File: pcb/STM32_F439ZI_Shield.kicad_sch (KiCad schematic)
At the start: 27 parts, among them J3 Relais_Conn, J4 Conn_01x02_Pin, J5 Conn_01x02_Pin, K1 G6S-2, K2 G6S-2, U1 LM2904, U12 FL25L16B, U13 R-78E-5.0-1.0, U2 MAX3485

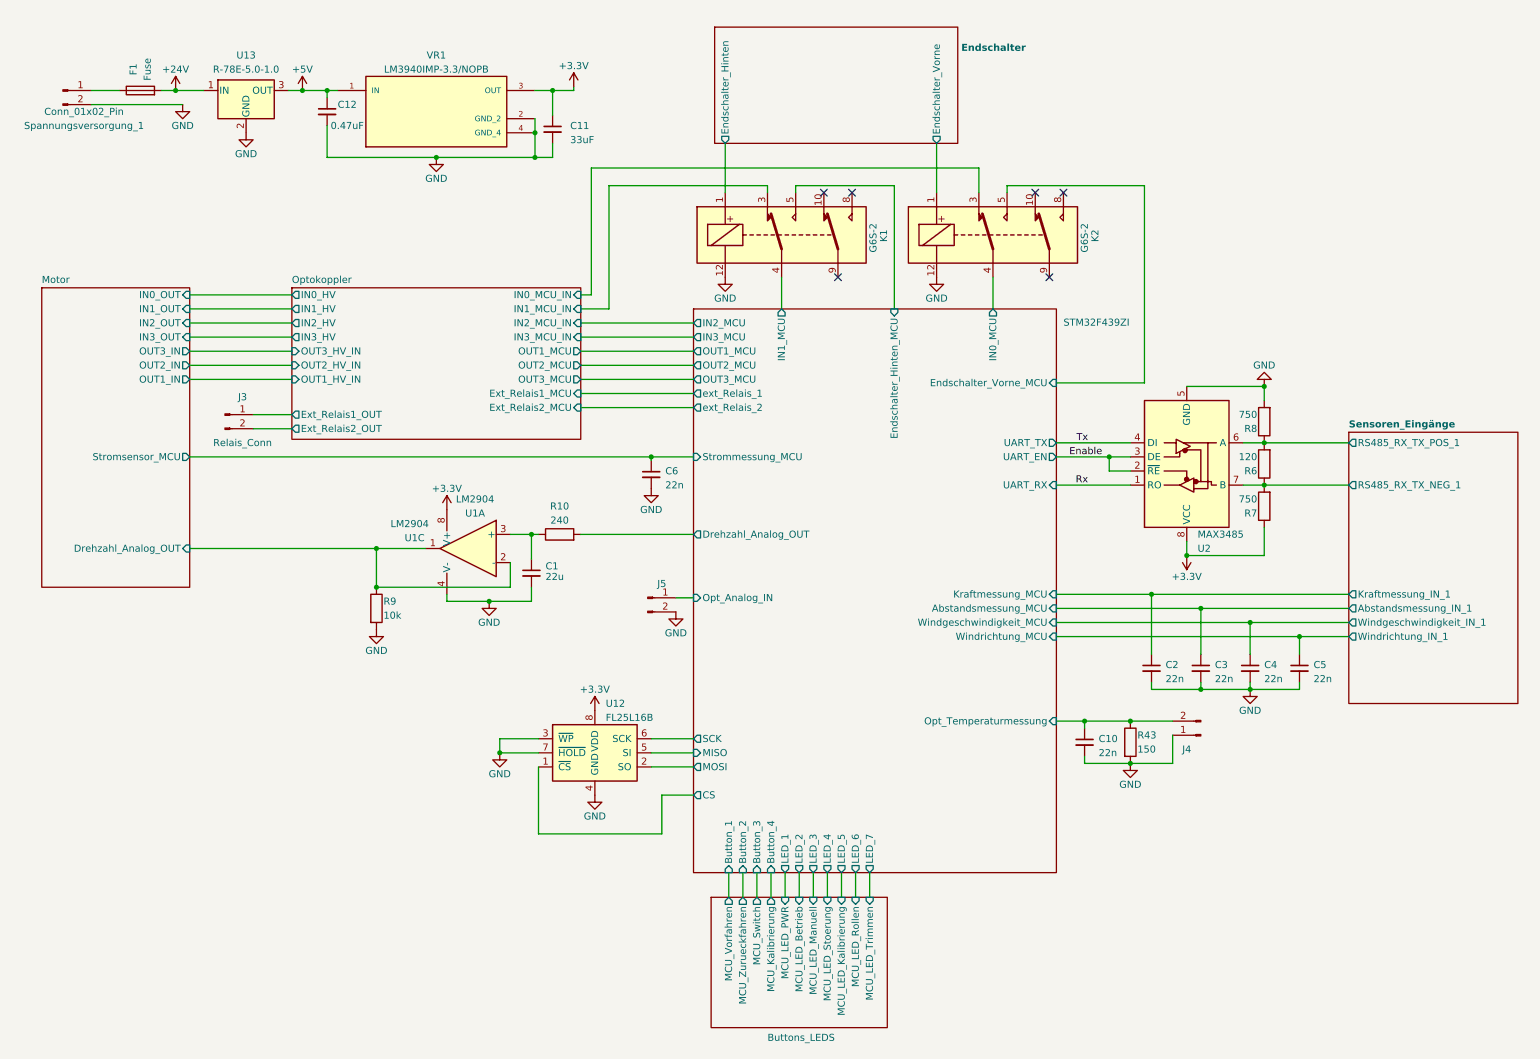
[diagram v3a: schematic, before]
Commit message: finished assigning pins and creating pcb
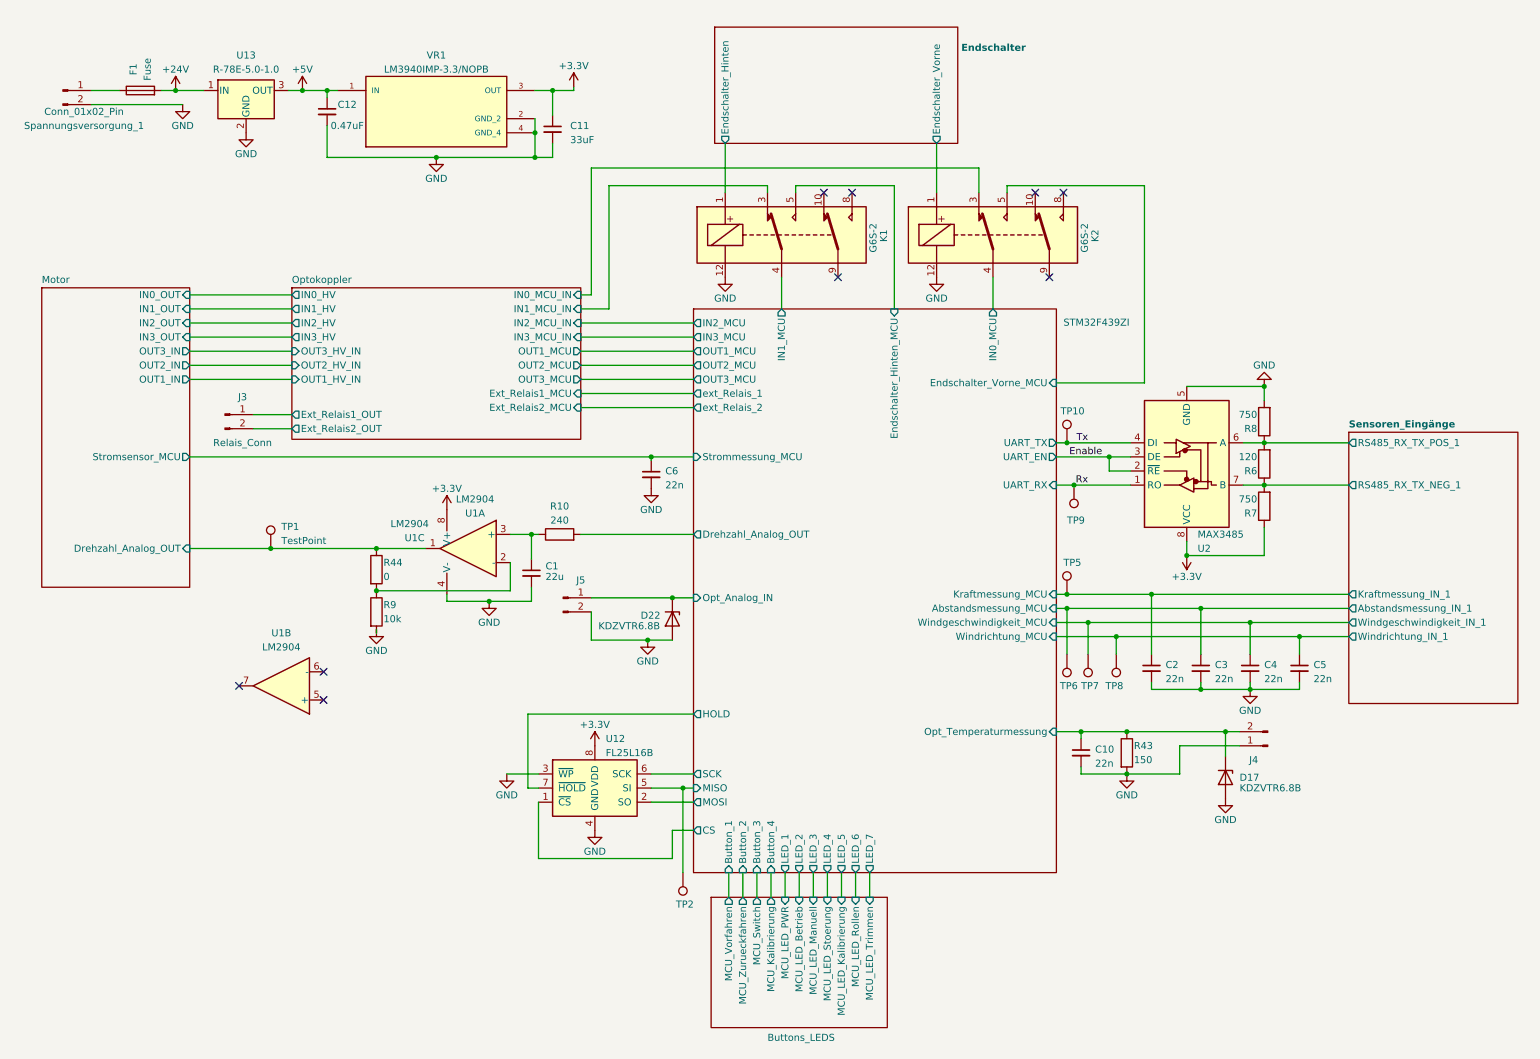
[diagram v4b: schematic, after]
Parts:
- added D17, D22: KDZVTR6.8B, Diode_SMD:D_SOD-123, symbol Diode:Z2SMBxxx
- added R44: 0, Resistor_SMD:R_1206_3216Metric, symbol Device:R
- added TP1, TP10, TP2, TP5, TP6, TP7, TP8, TP9: TestPoint, TestPoint:TestPoint_THTPad_2.0x2.0mm_Drill1.0mm, symbol Connector:TestPoint
- added unit 2 of U1
- Spannungsversorgung_1: footprint TerminalBlock_TE-Connectivity:TerminalBlock_TE_282834-2_1x02_P2.54mm_Horizontal -> TerminalBlock_Phoenix:TerminalBlock_Phoenix_PT-1,5-2-3.5-H_1x02_P3.50mm_Horizontal
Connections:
- net GND: now also D17.2 (A), D22.2 (A); no longer U12.7 (~{HOLD})
- net Motor/Drehzahl_Analog_OUT: now also R44.1, TP1.1; no longer R9.1, U1.2 (-)
- net Rx: now also TP9.1
- net STM32F439ZI/Abstandsmessung_MCU: now also TP6.1
- net STM32F439ZI/Kraftmessung_MCU: now also TP5.1
- net STM32F439ZI/MISO: now also TP2.1
- net STM32F439ZI/Opt_Analog_IN: now also D22.1 (K)
- net STM32F439ZI/Opt_Temperaturmessung: now also D17.1 (K)
- net STM32F439ZI/Windgeschwindigkeit_MCU: now also TP7.1
- net STM32F439ZI/Windrichtung_MCU: now also TP8.1
- net Tx: now also TP10.1
- new net: R44.2, R9.1, U1.2 (-)
- new net STM32F439ZI/HOLD: U12.7 (~{HOLD})
- no-connect marks 6 -> 9
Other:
- sheet Optokoppler: file untitled.kicad_sch -> Optokoppler.kicad_sch
- sheet STM32F439ZI ports: added HOLD; removed none
- moved on the sheet: C10, J4, J5, R43, R9, U12
